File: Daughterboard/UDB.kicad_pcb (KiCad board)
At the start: 4 copper layers, 18 x 16.5 mm, 13 parts, among them J1 TYPE-C-31-M12_13, J2 X1224WRS-04-LPV01, U1 TPD4E05U06DQAR

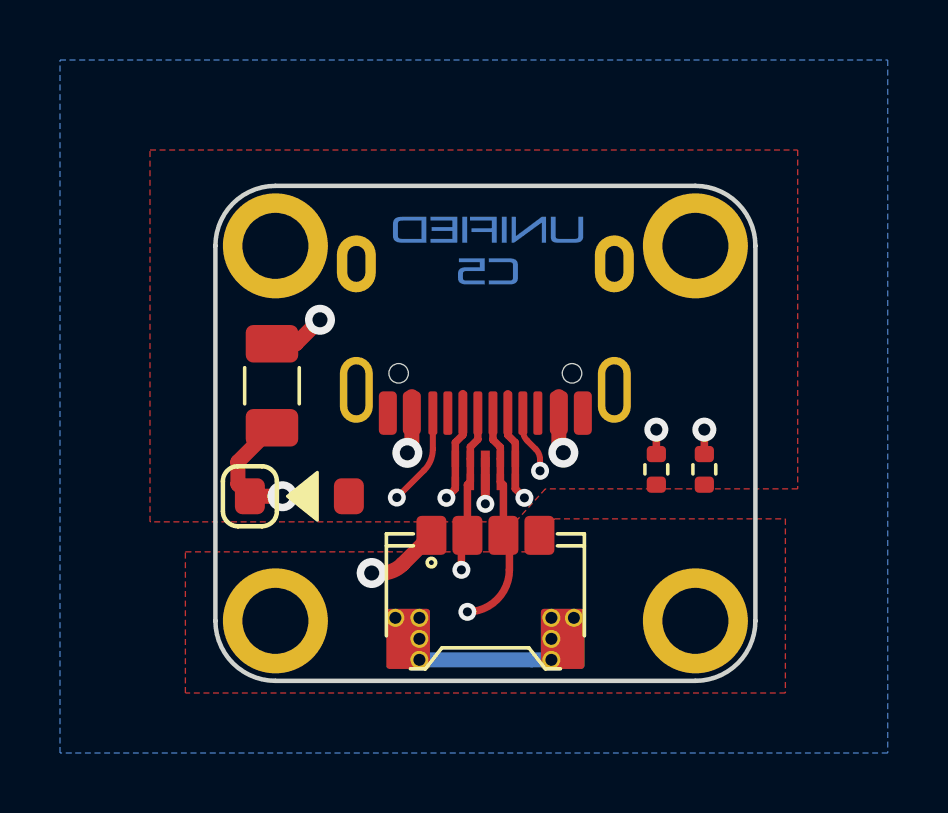
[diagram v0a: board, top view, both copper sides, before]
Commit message: daughterboard production
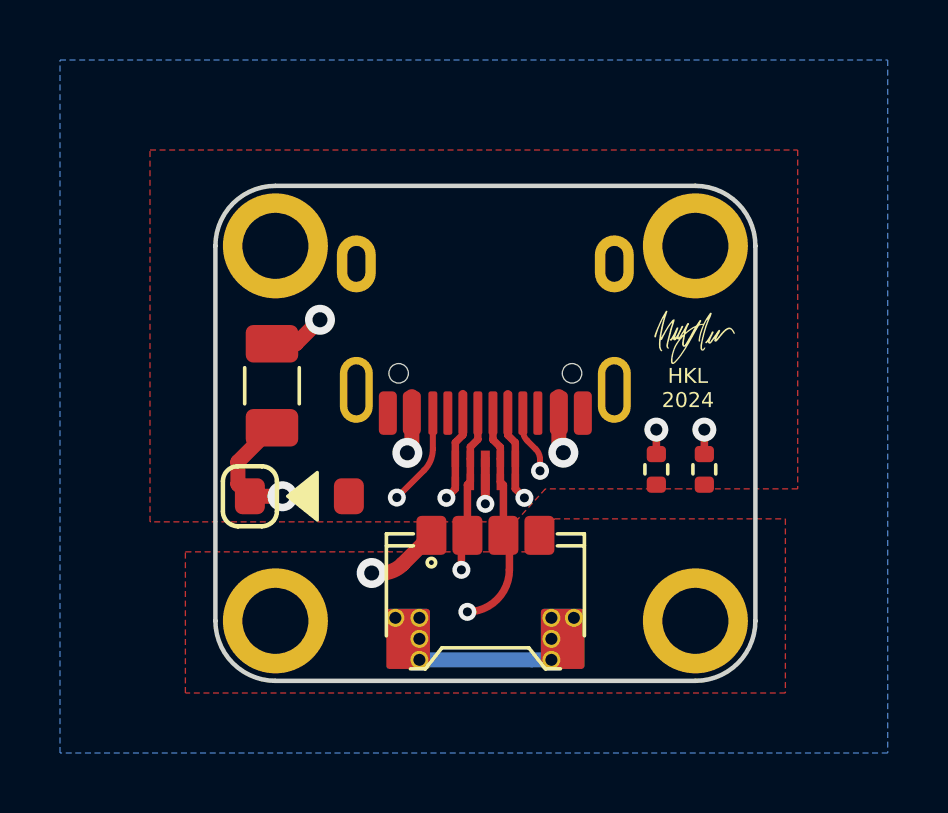
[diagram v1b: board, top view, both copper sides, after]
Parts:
- removed G1: Unified-Daughterboard-Logo, Unified-Daughterboard-Logo:Unified-Daughterboard-Logo.pretty
- removed G2: Unified-Daughterboard-Name, Unified-Daughterboard-Logo:Unified-Daughterboard-Name.pretty
- added G***: LOGO, LOGO, F.Cu at (82.0, 61.6)
- added G***: LOGO, LOGO, B.Cu at (74.8, 61.0)
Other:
- board text added: "HKL 2024"
- board text removed: "V5.0-EZM"
